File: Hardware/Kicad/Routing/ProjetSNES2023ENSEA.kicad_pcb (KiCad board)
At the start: 2 copper layers, 55 x 40 mm, 43 parts, among them J1 Conn_01x07_Socket, Q1 2N7002, Q2 2N7002, Q3 2N7002, SW1 SW_Push, U1 NRF24L01, U2 AMS1117-3.3, U3 STM32L412KBTx, Y1 16 MHz

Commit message: Updated Schematic & PCB
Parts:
- moved C3 1.47 mm to (81.0, 73.0)
- moved R1 1.47 mm to (83.0, 73.0)
- moved Antenna_nRF1 0.50 mm to (77.0, 68.5)
- renumbered D2 to D1, D1 to D2, R9 to R10, R10 to R9
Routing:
- net GND: track 17.0 -> 24.6 mm
- net Net-(U1-DVDD): track 0.00 -> 2.91 mm
- net Net-(U1-IREF): track 0.00 -> 2.65 mm
- net VDD_NRF: track 80.6 -> 78.9 mm, vias 6 -> 5

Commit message: Updated Schematic & PCB
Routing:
- net VDD_NRF: track 78.9 -> 96.2 mm, vias 5 -> 9
- net GND: track 24.6 -> 40.0 mm, vias 4 -> 8
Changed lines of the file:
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@@
   (segment (start 72.5 68.761827) (end 75.3 71.561827) (width 0.3) (layer "F.Cu") (net 3))
   (segment (start 54.95 92.11) (end 53.25 93.81) (width 0.3) (layer "F.Cu") (net 3))
+  (segment (start 82.0495 75.805928) (end 82.0495 76.513) (width 0.1) (layer "F.Cu") (net 3))
   (segment (start 65.0375 80.675) (end 63.8625 79.5) (width 0.3) (layer "F.Cu") (net 3))
   (segment (start 61.525 74.4125) (end 57.975 74.4125) (width 0.3) (layer "F.Cu") (net 3))
   (segment (start 62.722272 80.425) (end 60.075 80.425) (width 0.3) (layer "F.Cu") (net 3))
+  (segment (start 82.0495 76.513) (end 82 76.5625) (width 0.1) (layer "F.Cu") (net 3))
   (segment (start 63.647272 79.5) (end 62.722272 80.425) (width 0.3) (layer "F.Cu") (net 3))
+  (segment (start 81.5 80.4375) (end 81.5 81.102106) (width 0.1) (layer "F.Cu") (net 3))
   (segment (start 71.575 65.2875) (end 72.5 64.3625) (width 0.3) (layer "F.Cu") (net 3))
   (segment (start 61.525 70.4125) (end 57.975 70.4125) (width 0.3) (layer "F.Cu") (net 3))
+  (segment (start 81.5 81.102106) (end 81.310075 81.292031) (width 0.1) (layer "F.Cu") (net 3))
   (segment (start 71.575 67.4375) (end 71.575 65.2875) (width 0.3) (layer "F.Cu") (net 3))
   (segment (start 60.075 80.425) (end 59.15 79.5) (width 0.3) (layer "F.Cu") (net 3))
@@
   (segment (start 72.5 68.3625) (end 71.575 67.4375) (width 0.3) (layer "F.Cu") (net 3))
   (segment (start 59.15 79.5) (end 52.85 79.5) (width 0.3) (layer "F.Cu") (net 3))
+  (segment (start 83.638556 76.861444) (end 83.638556 77.201056) (width 0.1) (layer "F.Cu") (net 3))
   (segment (start 72.5 68.3625) (end 72.5 68.761827) (width 0.3) (layer "F.Cu") (net 3))
   (segment (start 69.7 79.911827) (end 69.7 80.675) (width 0.3) (layer "F.Cu") (net 3))
+  (segment (start 83.638556 77.201056) (end 83.9375 77.5) (width 0.1) (layer "F.Cu") (net 3))
   (segment (start 52.85 79.5) (end 54.95 81.6) (width 0.3) (layer "F.Cu") (net 3))
   (segment (start 61.525 66.4125) (end 57.975 66.4125) (width 0.3) (layer "F.Cu") (net 3))
@@
   (segment (start 75.3 74.311827) (end 69.7 79.911827) (width 0.3) (layer "F.Cu") (net 3))
   (segment (start 57.975 70.4125) (end 57.9375 70.45) (width 0.3) (layer "F.Cu") (net 3))
+  (via (at 82.0495 75.805928) (size 0.5) (drill 0.3) (layers "F.Cu" "B.Cu") (net 3))
+  (via (at 81.310075 81.292031) (size 0.5) (drill 0.3) (layers "F.Cu" "B.Cu") (net 3))
   (via (at 61.525 66.4125) (size 0.8) (drill 0.4) (layers "F.Cu" "B.Cu") (net 3))
   (via (at 61.525 70.4125) (size 0.8) (drill 0.4) (layers "F.Cu" "B.Cu") (net 3))
   (via (at 59.15 79.5) (size 0.8) (drill 0.4) (layers "F.Cu" "B.Cu") (net 3))
   (via (at 61.525 74.4125) (size 0.8) (drill 0.4) (layers "F.Cu" "B.Cu") (net 3))
+  (via (at 83.638556 76.861444) (size 0.5) (drill 0.3) (layers "F.Cu" "B.Cu") (net 3))
+  (via (at 75.3 74.311827) (size 0.5) (drill 0.3) (layers "F.Cu" "B.Cu") (net 3))
   (via (at 57.9375 74.45) (size 0.8) (drill 0.4) (layers "F.Cu" "B.Cu") (net 3))
+  (segment (start 76.794101 75.805928) (end 75.3 74.311827) (width 0.1) (layer "B.Cu") (net 3))
+  (segment (start 83.638556 78.96355) (end 83.638556 76.861444) (width 0.1) (layer "B.Cu") (net 3))
   (segment (start 61.525 74.4125) (end 61.525 70.4125) (width 0.3) (layer "B.Cu") (net 3))
+  (segment (start 83.105016 76.861444) (end 82.0495 75.805928) (width 0.1) (layer "B.Cu") (net 3))
   (segment (start 59.15 79.5) (end 59.15 75.6625) (width 0.3) (layer "B.Cu") (net 3))
+  (segment (start 81.310075 81.292031) (end 83.638556 78.96355) (width 0.1) (layer "B.Cu") (net 3))
   (segment (start 61.525 70.4125) (end 61.525 66.4125) (width 0.3) (layer "B.Cu") (net 3))
+  (segment (start 83.638556 76.861444) (end 83.105016 76.861444) (width 0.1) (layer "B.Cu") (net 3))
   (segment (start 59.15 75.6625) (end 57.9375 74.45) (width 0.3) (layer "B.Cu") (net 3))
+  (segment (start 82.0495 75.805928) (end 76.794101 75.805928) (width 0.1) (layer "B.Cu") (net 3))
   (segment (start 81.5 76.5625) (end 81.5 74.3625) (width 0.1) (layer "F.Cu") (net 4))
   (segment (start 81.5 74.3625) (end 81 73.8625) (width 0.1) (layer "F.Cu") (net 4))
@@
   (segment (start 75.576528 78.5) (end 78.725998 78.5) (width 0.1) (layer "B.Cu") (net 29))
   (segment (start 87 84.6375) (end 87 84.3625) (width 0.3) (layer "F.Cu") (net 49))
+  (segment (start 82.5995 75.321722) (end 82.4505 75.172722) (width 0.1) (layer "F.Cu") (net 49))
   (segment (start 73.375 63.5125) (end 72.5 62.6375) (width 0.3) (layer "F.Cu") (net 49))
+  (segment (start 82 81.58848) (end 81.997279 81.591201) (width 0.1) (layer "F.Cu") (net 49))
   (segment (start 72.5 66.6375) (end 73.375 65.7625) (width 0.3) (layer "F.Cu") (net 49))
+  (segment (start 82.5995 76.033746) (end 82.5995 75.321722) (width 0.1) (layer "F.Cu") (net 49))
+  (segment (start 84.533674 78) (end 83.9375 78) (width 0.1) (layer "F.Cu") (net 49))
   (segment (start 62.1375 79.5) (end 60.859502 79.5) (width 0.3) (layer "F.Cu") (net 49))
+  (segment (start 82 80.4375) (end 82 81.58848) (width 0.1) (layer "F.Cu") (net 49))
   (segment (start 60.859502 79.5) (end 60.849502 79.51) (width 0.3) (layer "F.Cu") (net 49))
   (segment (start 73.375 65.7625) (end 73.375 63.5125) (width 0.3) (layer "F.Cu") (net 49))
+  (segment (start 82.5 76.5625) (end 82.5 76.133246) (width 0.1) (layer "F.Cu") (net 49))
   (segment (start 87 84.3625) (end 88.8625 82.5) (width 0.3) (layer "F.Cu") (net 49))
+  (segment (start 81 75.305928) (end 80.9505 75.256428) (width 0.1) (layer "F.Cu") (net 49))
+  (segment (start 84.856837 77.676837) (end 84.533674 78) (width 0.1) (layer "F.Cu") (net 49))
+  (segment (start 81 76.5625) (end 81 75.305928) (width 0.1) (layer "F.Cu") (net 49))
+  (segment (start 82.5 76.133246) (end 82.5995 76.033746) (width 0.1) (layer "F.Cu") (net 49))
   (segment (start 59.15 81.8) (end 62.0875 81.8) (width 0.3) (layer "F.Cu") (net 49))
   (via (at 62.1375 77.2) (size 0.8) (drill 0.4) (layers "F.Cu" "B.Cu") (net 49))
   (via (at 60.849502 79.51) (size 0.8) (drill 0.4) (layers "F.Cu" "B.Cu") (net 49))
   (via (at 68.325 79.4495) (size 0.8) (drill 0.4) (layers "F.Cu" "B.Cu") (net 49))
+  (via (at 80.9505 75.256428) (size 0.5) (drill 0.3) (layers "F.Cu" "B.Cu") (net 49))
+  (via (at 81.997279 81.591201) (size 0.5) (drill 0.3) (layers "F.Cu" "B.Cu") (net 49))
   (via (at 62.0875 81.8) (size 0.8) (drill 0.4) (layers "F.Cu" "B.Cu") (net 49))
+  (via (at 84.856837 77.676837) (size 0.5) (drill 0.3) (layers "F.Cu" "B.Cu") (net 49))
+  (via (at 82.4505 75.172722) (size 0.5) (drill 0.3) (layers "F.Cu" "B.Cu") (net 49))
   (segment (start 60.849502 78.487998) (end 62.1375 77.2) (width 0.3) (layer "B.Cu") (net 49))
+  (segment (start 81.997279 81.591201) (end 84.856837 78.731643) (width 0.1) (layer "B.Cu") (net 49))
   (segment (start 60.849502 79.51) (end 60.849502 80.562002) (width 0.3) (layer "B.Cu") (net 49))
+  (segment (start 82.366794 75.256428) (end 82.4505 75.172722) (width 0.1) (layer "B.Cu") (net 49))
   (segment (start 60.849502 79.51) (end 60.849502 78.487998) (width 0.3) (layer "B.Cu") (net 49))
   (segment (start 60.849502 80.562002) (end 62.0875 81.8) (width 0.3) (layer "B.Cu") (net 49))
+  (segment (start 82.4505 75.172722) (end 82.727652 75.172722) (width 0.1) (layer "B.Cu") (net 49))
+  (segment (start 84.856837 78.731643) (end 84.856837 77.676837) (width 0.1) (layer "B.Cu") (net 49))
   (segment (start 66.0755 77.2) (end 68.325 79.4495) (width 0.3) (layer "B.Cu") (net 49))
+  (segment (start 80.9505 75.256428) (end 82.366794 75.256428) (width 0.1) (layer "B.Cu") (net 49))
+  (segment (start 82.727652 75.172722) (end 84.856837 77.301907) (width 0.1) (layer "B.Cu") (net 49))
   (segment (start 62.1375 77.2) (end 66.0755 77.2) (width 0.3) (layer "B.Cu") (net 49))
+  (segment (start 84.856837 77.301907) (end 84.856837 77.676837) (width 0.1) (layer "B.Cu") (net 49))
   (zone (net 49) (net_name "GND") (layer "F.Cu") (hatch edge 0.5)
     (priority 1)

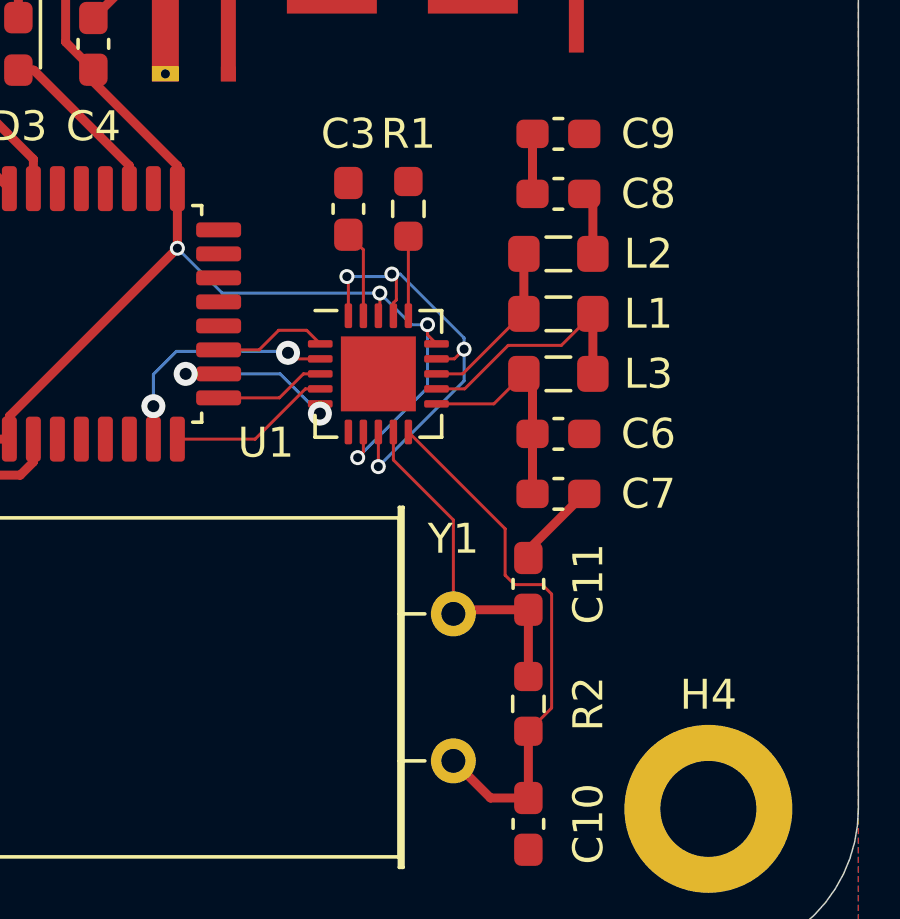
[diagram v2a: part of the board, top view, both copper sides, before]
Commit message: Updated Schematic & PCB (New netclasses / Antenna still need to be connected)
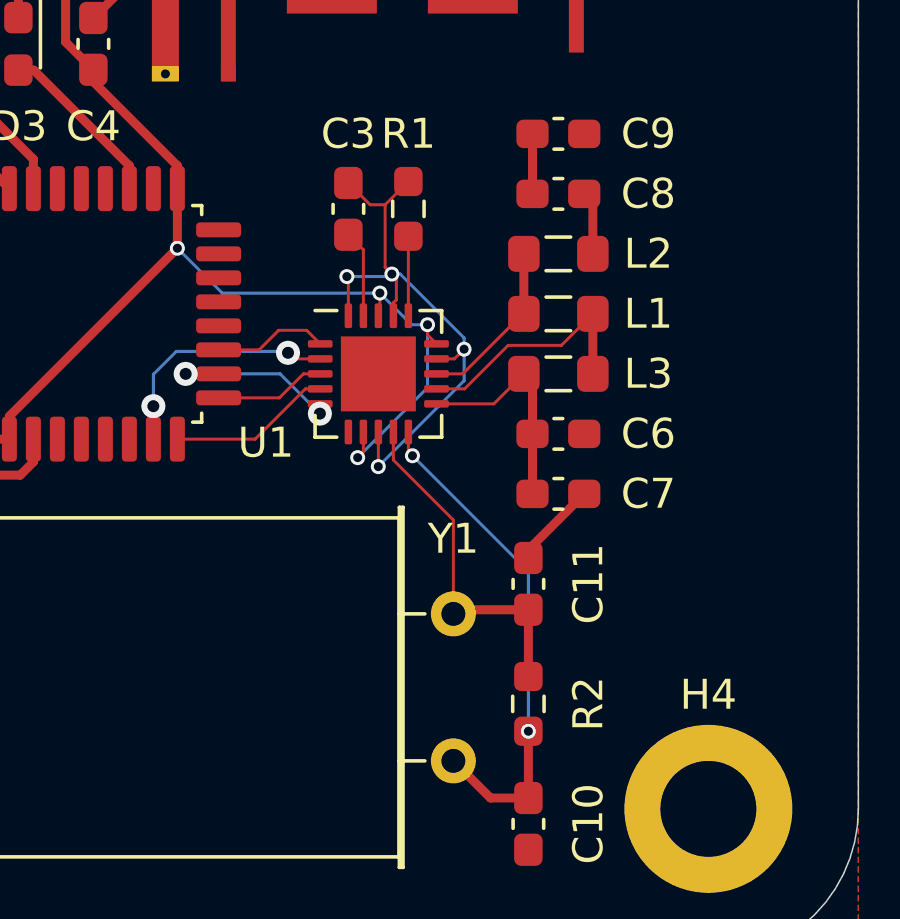
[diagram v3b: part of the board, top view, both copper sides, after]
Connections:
- Antenna_nRF1 pad 2: GND -> GND2
- C3 pad 2: GND -> GND1
- J1 pad 7: GND -> GND3
- R1 pad 2: GND -> GND1
- U1 pad 14: GND -> GND1
- U1 pad 17: GND -> GND1
- U1 pad 20: GND -> GND1
- U1 pad 8: GND -> GND1
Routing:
- net GND1: track 0.00 -> 20.3 mm, vias 0 -> 4
- net GND: track 40.0 -> 24.6 mm, vias 8 -> 4
- net XC1: track 18.1 -> 16.9 mm, vias 0 -> 2
